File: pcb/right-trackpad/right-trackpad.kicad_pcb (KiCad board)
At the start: 2 copper layers, 143 x 100 mm, 51 parts, among them SW1 SW_SPDT_312, SW2 SW_SPST, U1 SuperMini, U2 FFC&FPC_0.5mm_12pin

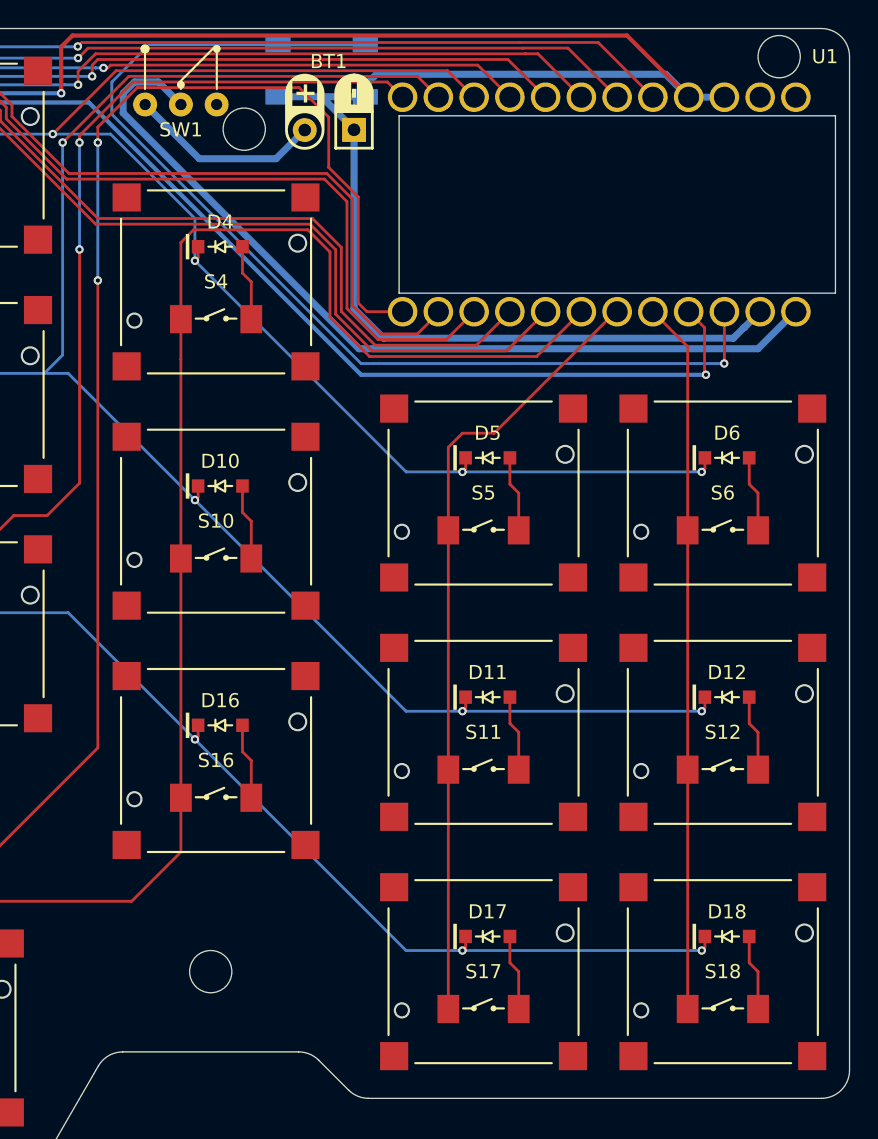
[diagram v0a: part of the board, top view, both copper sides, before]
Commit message: Add left half pcb draft
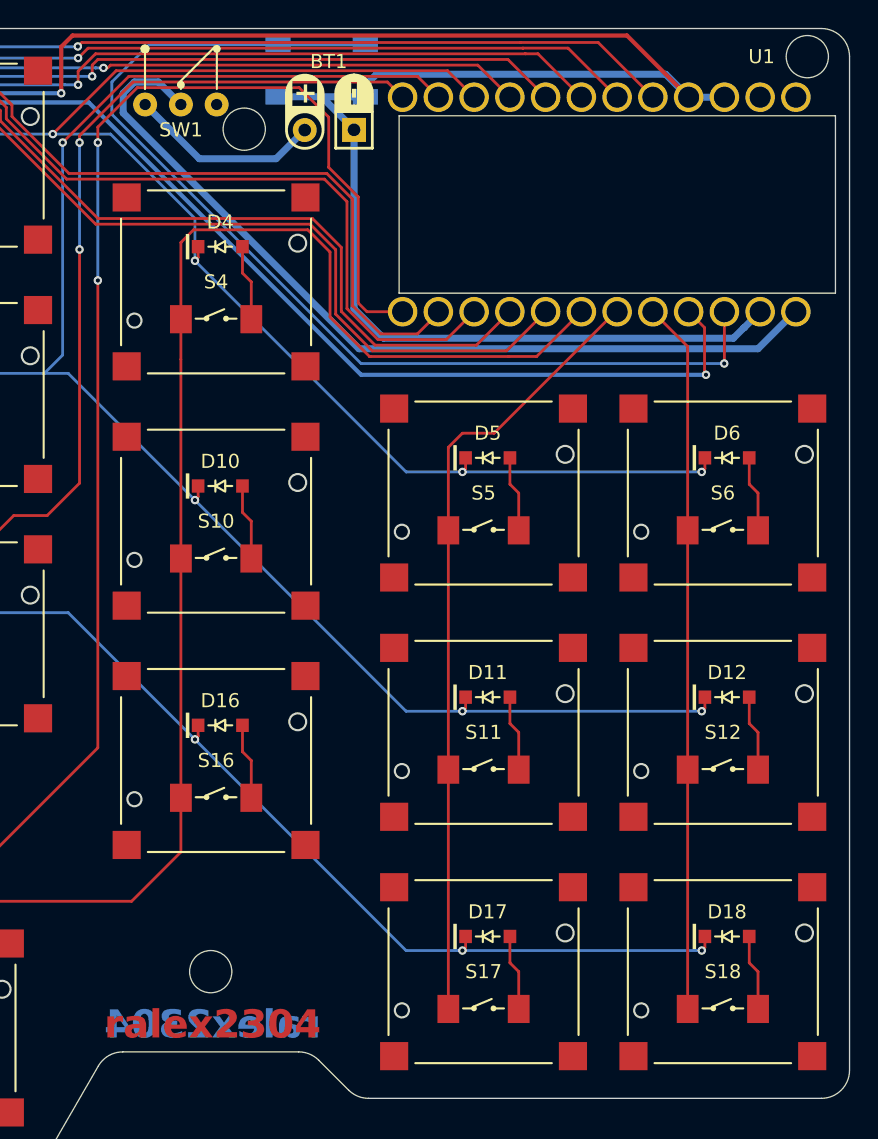
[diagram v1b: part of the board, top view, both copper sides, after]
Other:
- outline, holes or cut-outs redrawn
- board text added: "ralex2304"
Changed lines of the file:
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@@
 		(allow_soldermask_bridges_in_footprints no)
 		(tenting front back)
-		(grid_origin 218.5 52.35)
+		(grid_origin 215.5 52.35)
 		(pcbplotparams
 			(layerselection 0x00000000_00000000_55555555_5755f5ff)
@@
 		(tags "MCU")
 		(property "Reference" "U1"
-			(at -10.5 3.02 0)
+			(at -10.5 7.52 0)
 			(unlocked yes)
 			(layer "F.SilkS")
@@
 	)
 	(gr_circle
-		(center 215.5 52.35)
-		(end 217 52.35)
+		(center 217.5 52.35)
+		(end 219 52.35)
 		(stroke
 			(width 0.05)
@@
 		(layer "Edge.Cuts")
 	)
+	(gr_text "ralex2304"
+		(at 175.25 121.1 0)
+		(layer "F.Cu")
+		(effects
+			(font
+				(size 2 2)
+				(thickness 0.3)
+				(bold yes)
+			)
+		)
+	)
+	(gr_text "ralex2304"
+		(at 175.25 121.1 0)
+		(layer "B.Cu")
+		(effects
+			(font
+				(size 2 2)
+				(thickness 0.3)
+				(bold yes)
+			)
+			(justify mirror)
+		)
+	)
 	(gr_text "strizh"

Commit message: Change horizontal spacing and add nice!view to left half
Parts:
- moved D11 6.00 mm to (188.8, 97.8)
- moved D12 6.00 mm to (205.8, 97.8)
- moved D17 6.00 mm to (188.8, 114.8)
- moved D18 6.00 mm to (205.8, 114.8)
- moved D5 6.00 mm to (188.8, 80.8)
- moved D6 6.00 mm to (205.8, 80.8)
- moved S11 6.00 mm to (188.5, 100.3)
- moved S12 6.00 mm to (205.5, 100.3)
- moved S17 6.00 mm to (188.5, 117.3)
- moved S18 6.00 mm to (205.5, 117.3)
- moved S5 6.00 mm to (188.5, 83.3)
- moved S6 6.00 mm to (205.5, 83.3)
- moved SW2 6.00 mm to (177.0, 53.4)
- moved U1 5.94 mm to (215.8, 62.8)
- moved BT1 5.22 mm to (178.3, 55.9)
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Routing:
- net ROW4: track 202.5 -> 174.3 mm
- net COL4: track 137.0 -> 126.3 mm
- net dr: track 187.4 -> 177.0 mm
- net miso: track 193.8 -> 183.9 mm
- net sck: track 197.2 -> 187.3 mm
- net cs: track 184.6 -> 175.2 mm
- net mosi: track 189.8 -> 180.6 mm
- net -BATT: track 277.4 -> 268.7 mm
- net ROW1: track 151.1 -> 142.8 mm
- net COL5: track 152.2 -> 144.2 mm
- net ROW3: track 176.2 -> 168.8 mm
- net COL3: track 110.4 -> 103.4 mm
- net +3.3V: track 205.7 -> 199.2 mm
- net COL7: track 189.9 -> 184.3 mm
- net COL6: track 171.8 -> 166.3 mm
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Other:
- board size 143 x 100 mm -> 137 x 100 mm

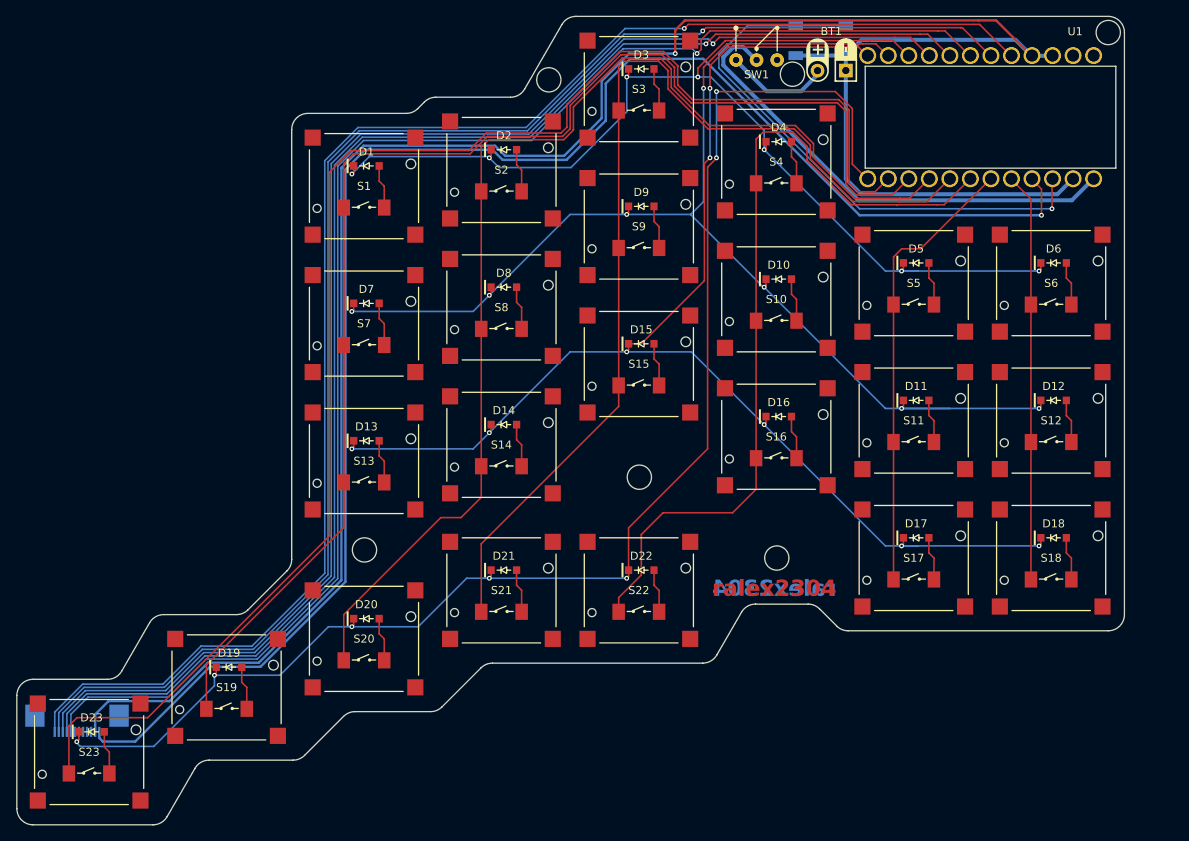
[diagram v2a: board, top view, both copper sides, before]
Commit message: Add vias to switch footprints
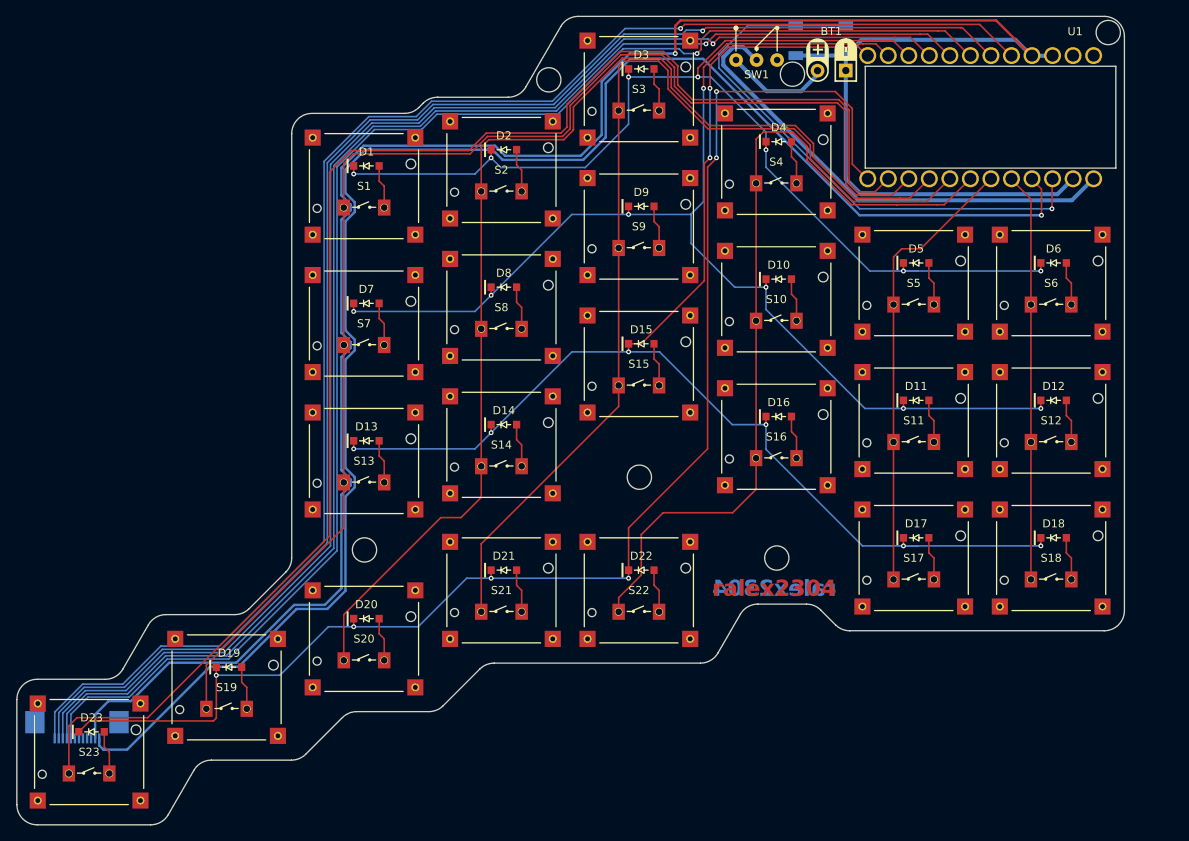
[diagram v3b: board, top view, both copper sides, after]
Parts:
- moved U2 0.80 mm to (85.0, 140.3)
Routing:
- net -BATT: track 268.7 -> 274.6 mm
- net +3.3V: track 199.2 -> 204.5 mm
- net ROW2: track 155.9 -> 153.1 mm
- net sck: track 187.3 -> 185.9 mm
- net ROW1: track 142.8 -> 144.2 mm
- net miso: track 183.9 -> 182.6 mm
- net ROW3: track 168.8 -> 170.1 mm
- net mosi: track 180.6 -> 179.5 mm
- net dr: track 177.0 -> 176.2 mm
- net cs: track 175.2 -> 174.4 mm
- net ROW4: track 174.3 -> 173.9 mm, vias 7 -> 6
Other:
- outline, holes or cut-outs redrawn

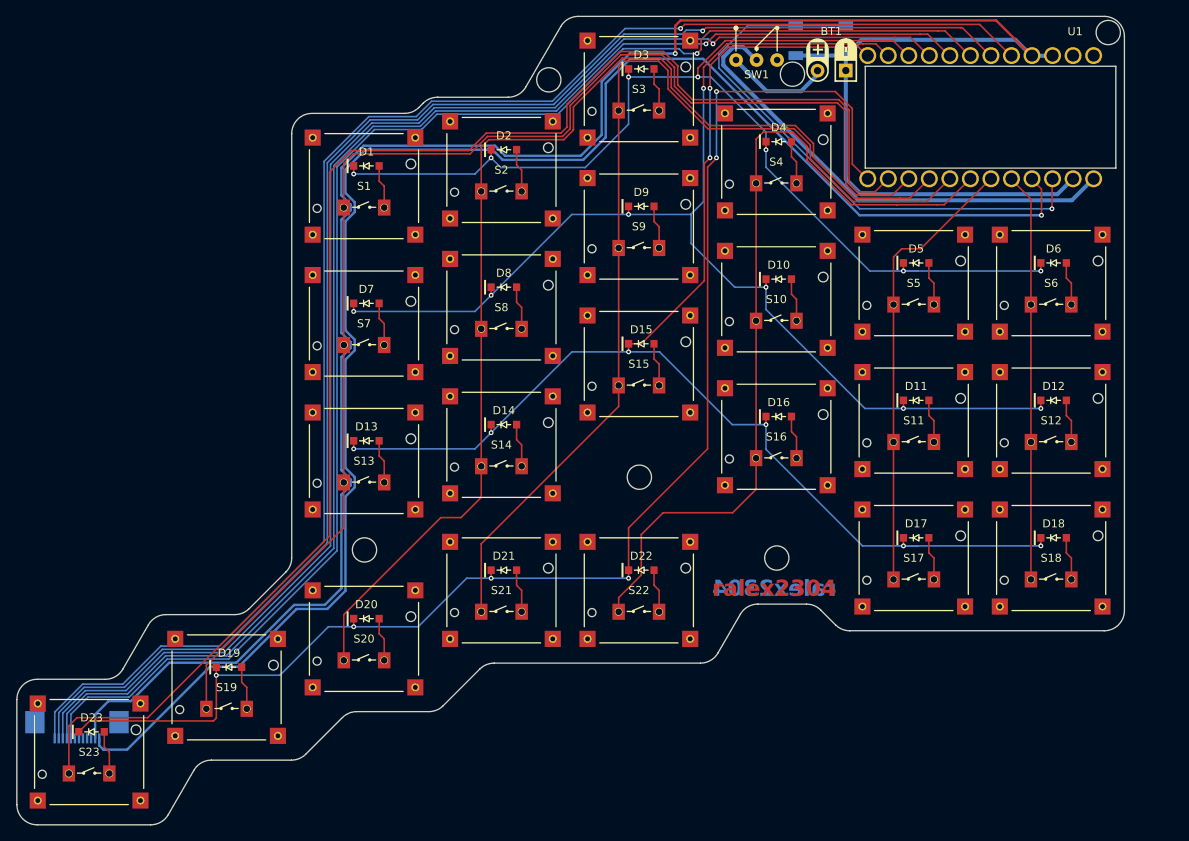
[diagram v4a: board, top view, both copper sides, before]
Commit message: Fix slight shift, enlarge vias to meet manufacturing requirements
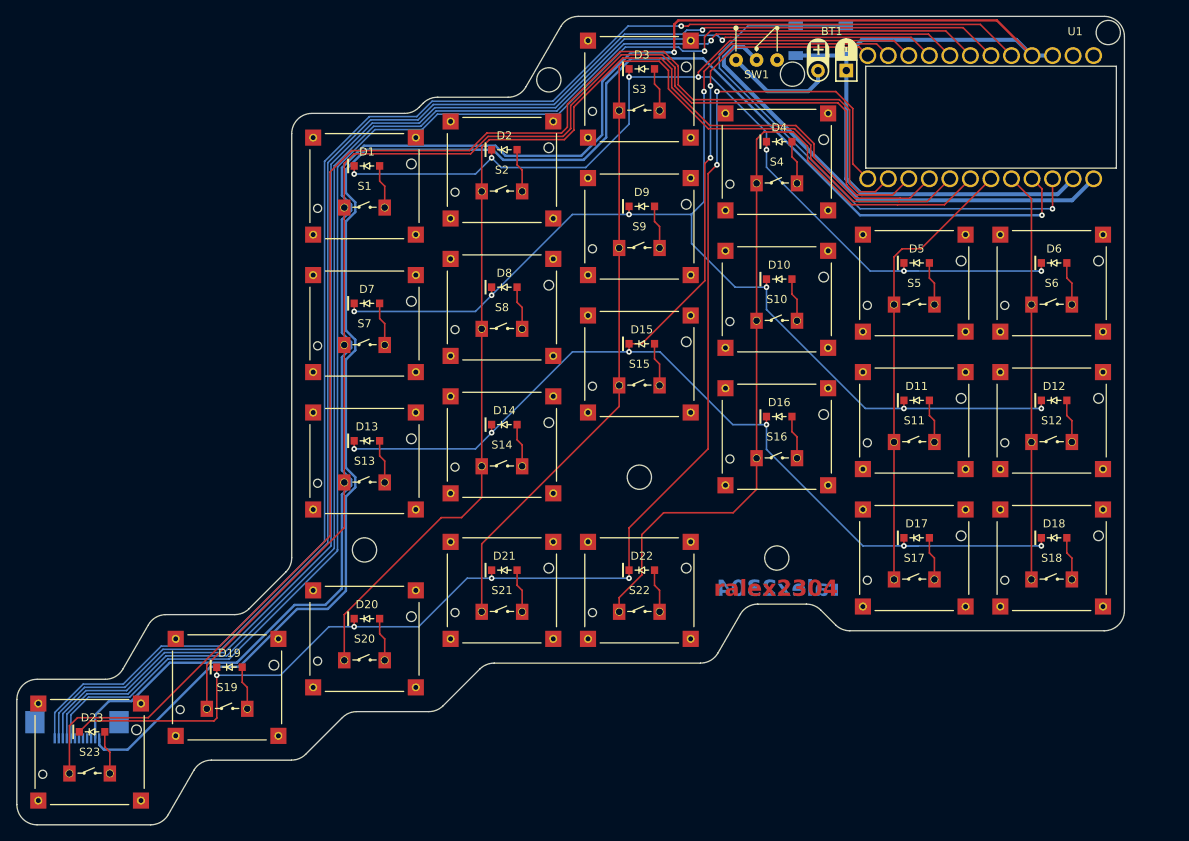
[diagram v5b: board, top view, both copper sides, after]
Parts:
- moved D1 0.06 mm to (120.9, 68.8)
- moved D13 0.06 mm to (120.9, 102.8)
- moved D19 0.06 mm to (103.9, 130.8)
- moved D20 0.06 mm to (120.9, 124.8)
- moved D23 0.06 mm to (86.9, 138.8)
- moved D7 0.06 mm to (120.9, 85.8)
- moved S1 0.06 mm to (120.6, 71.3)
- moved S10 0.06 mm to (171.6, 85.3)
- moved S11 0.06 mm to (188.6, 100.3)
- moved S12 0.06 mm to (205.6, 100.3)
- moved S13 0.06 mm to (120.6, 105.3)
- moved S14 0.06 mm to (137.6, 103.3)
- moved S15 0.06 mm to (154.6, 93.3)
- moved S16 0.06 mm to (171.6, 102.3)
- moved S17 0.06 mm to (188.6, 117.3)
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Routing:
- net +BATT: track 12.6 -> 13.6 mm
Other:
- outline, holes or cut-outs redrawn
